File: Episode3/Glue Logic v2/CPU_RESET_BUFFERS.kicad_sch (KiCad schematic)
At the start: 28 parts, among them SW1 RST SW, U1 HD63C09P, U2 MIC1232, U3 74HCT541, U4 74HCT541, U5 74HCT245, U6 74HCT125, X1 12MHz

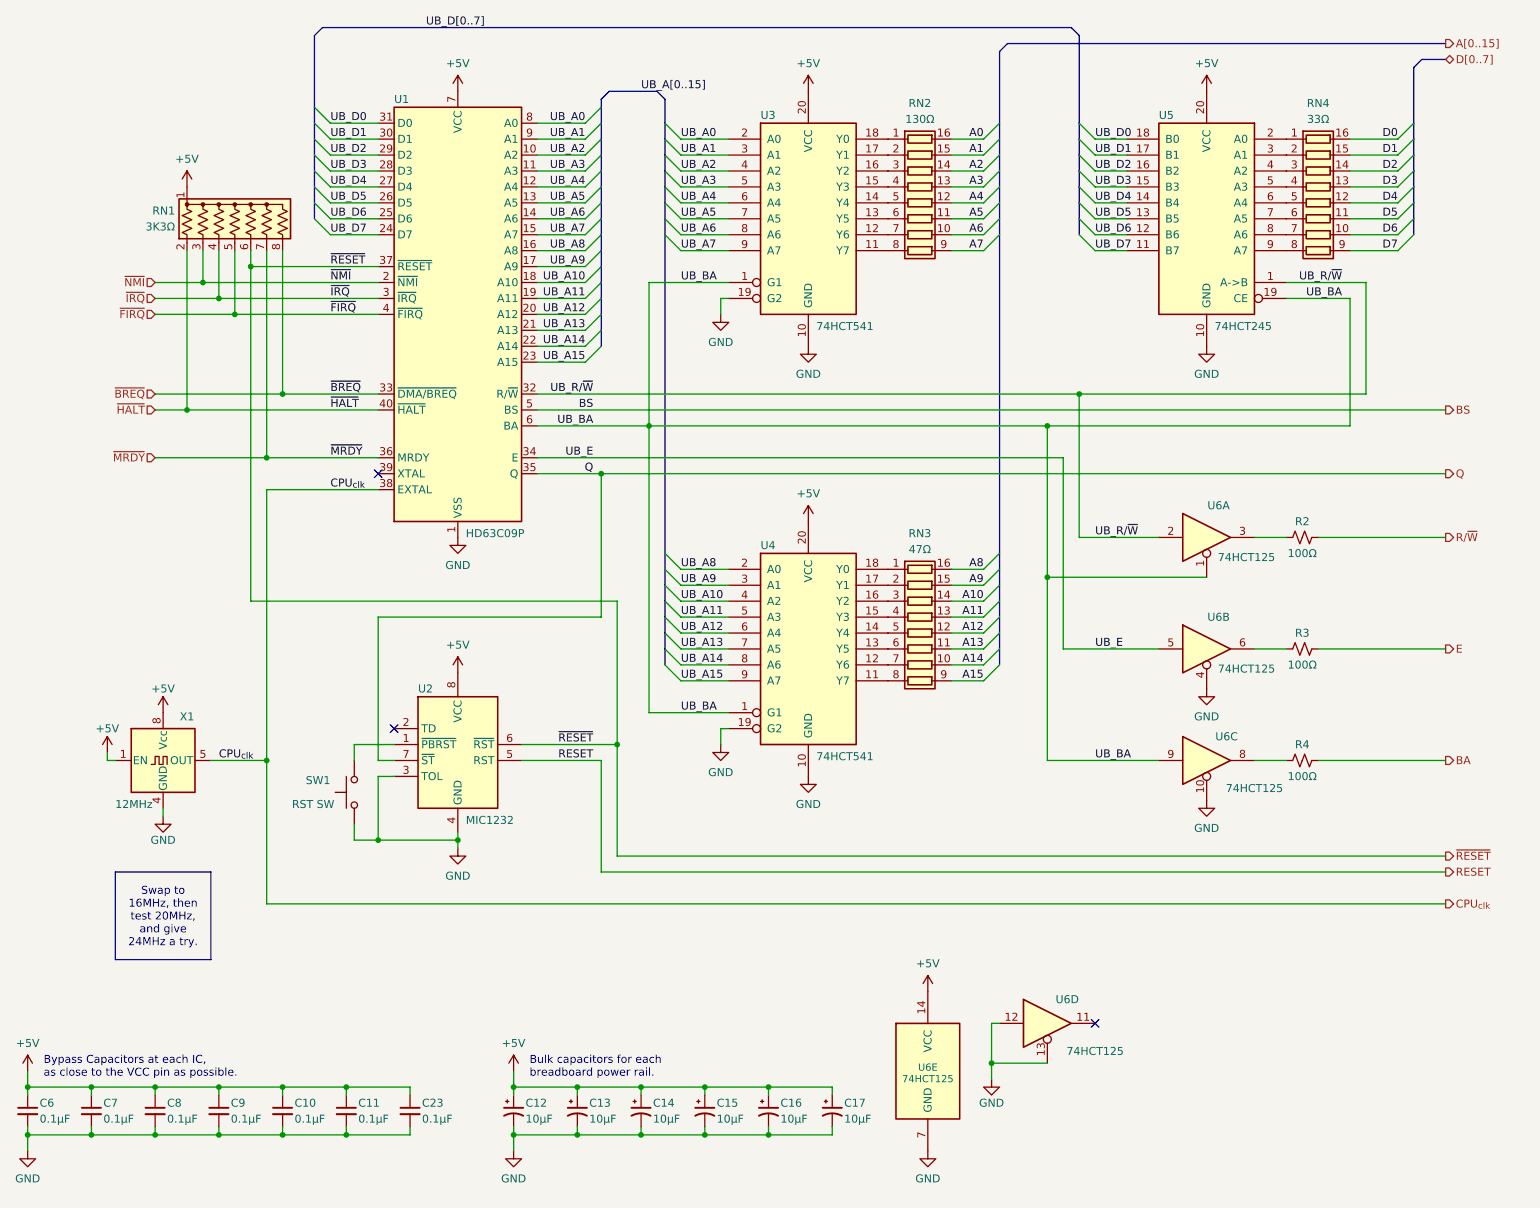
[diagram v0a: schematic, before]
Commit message: changed strategy and simplified things
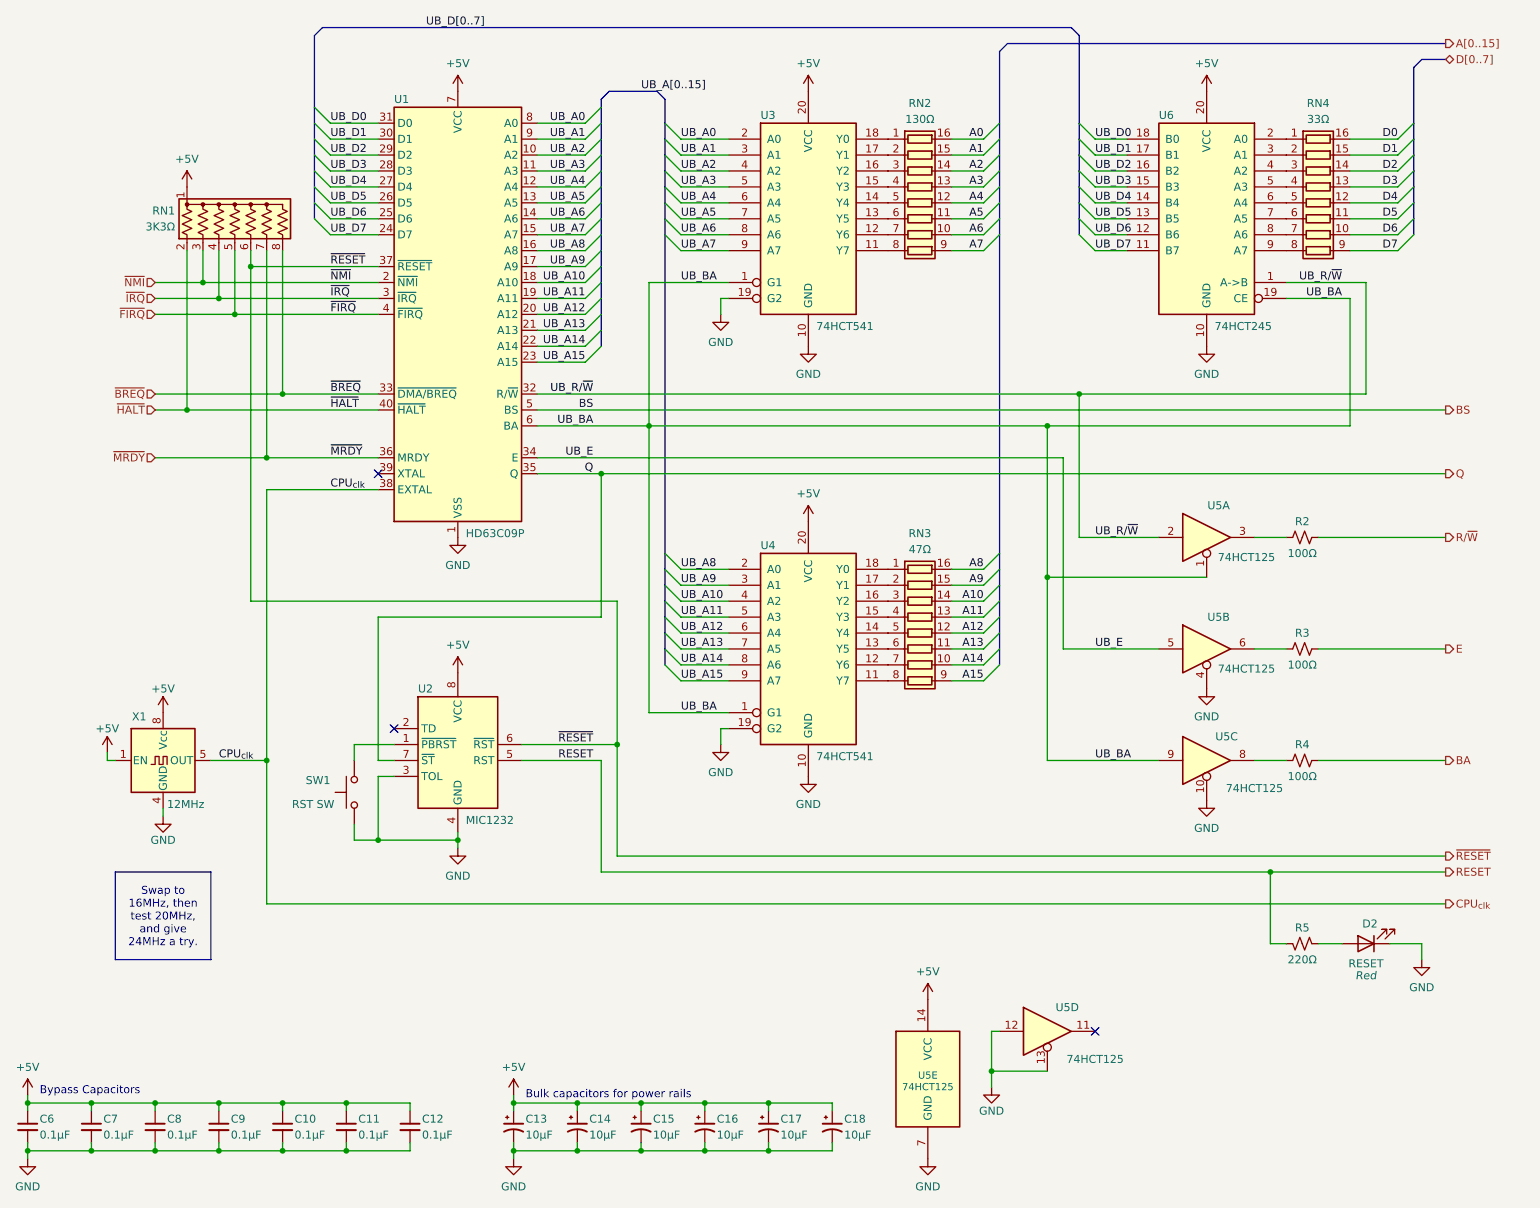
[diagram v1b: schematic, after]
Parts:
- added D2: RESET, symbol Device:LED
- added R5: 220Ω, symbol Device:R_Small_US
- renumbered C23 to C12, C12 to C13, C13 to C14, C14 to C15, C15 to C16, C16 to C17, C17 to C18, U6 to U5, U5 to U6
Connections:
- net GND: now also D2.1 (K)
- net RESET: now also R5.1
- new net: D2.2 (A), R5.2
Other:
- note added: "Bulk capacitors for power rails"
- note added: "Bypass Capacitors"
- note removed: "Bulk capacitors for each breadboard power rail."
- note removed: "Bypass Capacitors at each IC, as close to the VCC pin as possible."
- moved on the sheet: C10, C11, C12, C13, C14, C15, C16, C17, C18, C6, C7, C8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
